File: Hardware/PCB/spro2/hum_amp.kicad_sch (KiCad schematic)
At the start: 5 parts, among them U4 ${SIM.PARAMS}

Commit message: Updated schematic and 1st version of the PCB
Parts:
- removed U4: ${SIM.PARAMS}, symbol Simulation_SPICE:OPAMP
- added C3: 4.7u, Capacitor_THT:CP_Radial_D5.0mm_P2.00mm, symbol Device:C
- added R4: 3.3, Resistor_THT:R_Axial_DIN0207_L6.3mm_D2.5mm_P10.16mm_Horizontal, symbol Device:R
- added U3: TL074, SPRO_lib:DIP794W53P254L1930H508Q14N, symbol Amplifier_Operational:TL074
- R5: renamed from R4; footprint (none) -> Resistor_THT:R_Axial_DIN0207_L6.3mm_D2.5mm_P10.16mm_Horizontal
- R6: renamed from R5; footprint (none) -> Resistor_THT:R_Axial_DIN0207_L6.3mm_D2.5mm_P10.16mm_Horizontal
- R7: renamed from R6; footprint (none) -> Resistor_THT:R_Axial_DIN0207_L6.3mm_D2.5mm_P10.16mm_Horizontal
- R8: renamed from R7; footprint (none) -> Resistor_THT:R_Axial_DIN0207_L6.3mm_D2.5mm_P10.16mm_Horizontal
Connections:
- net GND: now also C3.2
- net Hum_Amp__Out: now also U3.14
- net Humidity_In: now also R4.1; no longer R6.1
- net at R7.2, R8.1: now also U3.12 (+)
- net at R5.2, R6.2: now also U3.13 (-)
- new net: C3.1, R4.2, R6.1

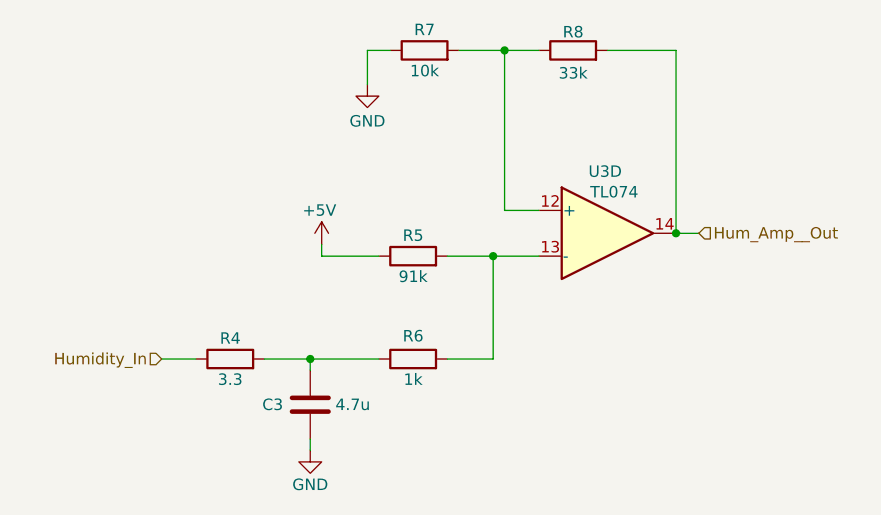
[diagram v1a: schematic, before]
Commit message: Changes to humidity circuit. Add MAX660 circuit
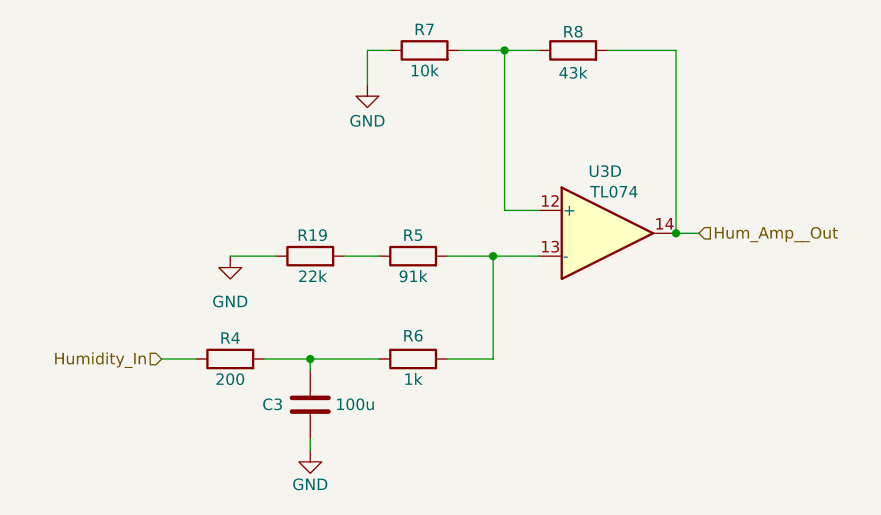
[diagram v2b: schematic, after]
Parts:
- added R19: 22k, symbol Device:R
- C3: value 4.7u -> 100u
- R4: value 3.3 -> 200
- R8: value 33k -> 43k
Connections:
- net GND: now also R19.1
- net +5V: no longer names the net of R5.1
- net +5V: now also R19.2
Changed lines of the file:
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@@
-	(wire
-		(pts
-			(xy 130.81 91.44) (xy 137.16 91.44)
-		)
-		(stroke
-			(width 0)
-			(type default)
-		)
-	)
 	(wire
 		(pts
@@
 	(wire
 		(pts
+			(xy 133.35 91.44) (xy 137.16 91.44)
+		)
+		(stroke
+			(width 0)
+			(type default)
+		)
+	)
+	(wire
+		(pts
 			(xy 124.46 102.87) (xy 129.54 102.87)
 		)
@@
 	(wire
 		(pts
-			(xy 130.81 90.17) (xy 130.81 91.44)
-		)
-		(stroke
-			(width 0)
-			(type default)
-		)
-	)
-	(wire
-		(pts
 			(xy 135.89 68.58) (xy 138.43 68.58)
 		)
@@
 		(pts
 			(xy 113.03 102.87) (xy 116.84 102.87)
+		)
+		(stroke
+			(width 0)
+			(type default)
+		)
+	)
+	(wire
+		(pts
+			(xy 120.65 91.44) (xy 125.73 91.44)
 		)
 		(stroke
@@
 	)
 	(symbol
+		(lib_id "power:GND")
+		(at 120.65 91.44 0)
+		(unit 1)
+		(exclude_from_sim no)
+		(in_bom yes)
+		(on_board yes)
+		(dnp no)
+		(fields_autoplaced yes)
+		(property "Reference" "#PWR017"
+			(at 120.65 97.79 0)
+			(effects
+				(font
+					(size 1.27 1.27)
+				)
+				(hide yes)
+			)
+		)
+		(property "Value" "GND"
+			(at 120.65 96.52 0)
+			(effects
+				(font
+					(size 1.27 1.27)
+				)
+			)
+		)
+		(property "Footprint" ""
+			(at 120.65 91.44 0)
+			(effects
+				(font
+					(size 1.27 1.27)
+				)
+				(hide yes)
+			)
+		)
+		(property "Datasheet" ""
+			(at 120.65 91.44 0)
+			(effects
+				(font
+					(size 1.27 1.27)
+				)
+				(hide yes)
+			)
+		)
+		(property "Description" "Power symbol creates a global label with name \"GND\" , ground"
+			(at 120.65 91.44 0)
+			(effects
+				(font
+					(size 1.27 1.27)
+				)
+				(hide yes)
+			)
+		)
+		(pin "1"
+		)
+		(instances
+			(project ""
+				(path "/edfea366-2226-45cc-893f-1155e0ffe333/714514db-32eb-40cc-b906-bb659214b924"
+					(reference "#PWR017")
+					(unit 1)
+				)
+			)
+		)
+	)
+	(symbol
 		(lib_id "Amplifier_Operational:TL074")
 		(at 162.56 88.9 0)
@@
 	)
 	(symbol
-		(lib_id "power:+5V")
-		(at 130.81 90.17 0)
-		(unit 1)
-		(exclude_from_sim no)
-		(in_bom yes)
-		(on_board yes)
-		(dnp no)
-		(property "Reference" "#PWR017"
-			(at 130.81 93.98 0)
-			(effects
-				(font
-					(size 1.27 1.27)
-				)
-				(hide yes)
-			)
-		)
-		(property "Value" "+5V"
-			(at 130.556 86.36 0)
-			(effects
-				(font
-					(size 1.27 1.27)
-				)
-			)
-		)
-		(property "Footprint" ""
-			(at 130.81 90.17 0)
-			(effects
-				(font
-					(size 1.27 1.27)
-				)
-				(hide yes)
-			)
-		)
-		(property "Datasheet" ""
-			(at 130.81 90.17 0)
-			(effects
-				(font
-					(size 1.27 1.27)
-				)
-				(hide yes)
-			)
-		)
-		(property "Description" "Power symbol creates a global label with name \"+5V\""
-			(at 130.81 90.17 0)
-			(effects
-				(font
-					(size 1.27 1.27)
-				)
-				(hide yes)
-			)
-		)
-		(pin "1"
-		)
-		(instances
-			(project "spro2"
-				(path "/edfea366-2226-45cc-893f-1155e0ffe333/714514db-32eb-40cc-b906-bb659214b924"
-					(reference "#PWR017")
-					(unit 1)
-				)
-			)
-		)
-	)
-	(symbol
 		(lib_id "power:GND")
 		(at 135.89 72.39 0)
@@
 	)
 	(symbol
+		(lib_id "Device:R")
+		(at 129.54 91.44 90)
+		(unit 1)
+		(exclude_from_sim no)
+		(in_bom yes)
+		(on_board yes)
+		(dnp no)
+		(property "Reference" "R19"
+			(at 129.794 89.154 90)
+			(effects
+				(font
+					(size 1.27 1.27)
+				)
+			)
+		)
+		(property "Value" "22k"
+			(at 129.794 93.726 90)
+			(effects
+				(font
+					(size 1.27 1.27)
+				)
+			)
+		)
+		(property "Footprint" ""
+			(at 129.54 93.218 90)
+			(effects
+				(font
+					(size 1.27 1.27)
+				)
+				(hide yes)
+			)
+		)
+		(property "Datasheet" "~"
+			(at 129.54 91.44 0)
+			(effects
+				(font
+					(size 1.27 1.27)
+				)
+				(hide yes)
+			)
+		)
+		(property "Description" "Resistor"
+			(at 129.54 91.44 0)
+			(effects
+				(font
+					(size 1.27 1.27)
+				)
+				(hide yes)
+			)
+		)
+		(pin "1"
+		)
+		(pin "2"
+		)
+		(instances
+			(project ""
+				(path "/edfea366-2226-45cc-893f-1155e0ffe333/714514db-32eb-40cc-b906-bb659214b924"
+					(reference "R19")
+					(unit 1)
+				)
+			)
+		)
+	)
+	(symbol
 		(lib_id "Device:C")
 		(at 129.54 107.95 0)
@@
 			)
 		)
-		(property "Value" "4.7u"
+		(property "Value" "100u"
 			(at 132.334 107.95 0)
 			(effects
@@
 			)
 		)
-		(property "Value" "33k"
+		(property "Value" "43k"
 			(at 158.75 71.12 90)
 			(effects
@@
 			)
 		)
-		(property "Value" "3.3"
+		(property "Value" "200"
 			(at 120.65 105.156 90)
 			(effects

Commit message: Hopefully last version of PCB
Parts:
- removed C3: 100u, Capacitor_THT:CP_Radial_D5.0mm_P2.00mm, symbol Device:C
- added C7: 100u, Capacitor_THT:CP_Radial_D10.0mm_P5.00mm, symbol Device:C_Polarized
- R6: renamed from R19; footprint (none) -> Resistor_THT:R_Axial_DIN0207_L6.3mm_D2.5mm_P10.16mm_Horizontal
- renumbered R8 to R10, R4 to R5, R5 to R7, R6 to R8, R7 to R9
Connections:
- net GND: now also C7.2
- net at R5.2, R8.1: now also C7.1
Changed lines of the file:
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@@
+	)
+	(symbol
+		(lib_id "Device:C_Polarized")
+		(at 129.54 107.95 0)
+		(unit 1)
+		(exclude_from_sim no)
+		(in_bom yes)
+		(on_board yes)
+		(dnp no)
+		(fields_autoplaced yes)
+		(property "Reference" "C7"
+			(at 133.35 105.7909 0)
+			(effects
+				(font
+					(size 1.27 1.27)
+				)
+				(justify left)
+			)
+		)
+		(property "Value" "100u"
+			(at 133.35 108.3309 0)
+			(effects
+				(font
+					(size 1.27 1.27)
+				)
+				(justify left)
+			)
+		)
+		(property "Footprint" "Capacitor_THT:CP_Radial_D10.0mm_P5.00mm"
+			(at 130.5052 111.76 0)
+			(effects
+				(font
+					(size 1.27 1.27)
+				)
+				(hide yes)
+			)
+		)
+		(property "Datasheet" "~"
+			(at 129.54 107.95 0)
+			(effects
+				(font
+					(size 1.27 1.27)
+				)
+				(hide yes)
+			)
+		)
+		(property "Description" "Polarized capacitor"
+			(at 129.54 107.95 0)
+			(effects
+				(font
+					(size 1.27 1.27)
+				)
+				(hide yes)
+			)
+		)
+		(pin "1"
+		)
+		(pin "2"
+		)
+		(instances
+			(project "spro2"
+				(path "/edfea366-2226-45cc-893f-1155e0ffe333/714514db-32eb-40cc-b906-bb659214b924"
+					(reference "C7")
+					(unit 1)
+				)
+			)
+		)
 	)
 	(symbol
@@
 		(on_board yes)
 		(dnp no)
-		(property "Reference" "#PWR016"
+		(property "Reference" "#PWR018"
 			(at 129.54 119.38 0)
 			(effects
@@
 			(project "spro2"
 				(path "/edfea366-2226-45cc-893f-1155e0ffe333/714514db-32eb-40cc-b906-bb659214b924"
-					(reference "#PWR016")
+					(reference "#PWR018")
 					(unit 1)
 				)
@@
 		(on_board yes)
 		(dnp no)
-		(property "Reference" "#PWR018"
+		(property "Reference" "#PWR019"
 			(at 135.89 78.74 0)
 			(effects
@@
 			(project "spro2"
 				(path "/edfea366-2226-45cc-893f-1155e0ffe333/714514db-32eb-40cc-b906-bb659214b924"
-					(reference "#PWR018")
+					(reference "#PWR019")
 					(unit 1)
 				)
@@
 		(on_board yes)
 		(dnp no)
-		(property "Reference" "R19"
+		(property "Reference" "R6"
 			(at 129.794 89.154 90)
 			(effects
@@
 			)
 		)
-		(property "Footprint" ""
+		(property "Footprint" "Resistor_THT:R_Axial_DIN0207_L6.3mm_D2.5mm_P10.16mm_Horizontal"
 			(at 129.54 93.218 90)
 			(effects
@@
 			(project ""
 				(path "/edfea366-2226-45cc-893f-1155e0ffe333/714514db-32eb-40cc-b906-bb659214b924"
-					(reference "R19")
-					(unit 1)
-				)
-			)
-		)
-	)
-	(symbol
-		(lib_id "Device:C")
-		(at 129.54 107.95 0)
-		(unit 1)
-		(exclude_from_sim no)
-		(in_bom yes)
-		(on_board yes)
-		(dnp no)
-		(property "Reference" "C3"
-			(at 124.206 107.95 0)
-			(effects
-				(font
-					(size 1.27 1.27)
-				)
-				(justify left)
-			)
-		)
-		(property "Value" "100u"
-			(at 132.334 107.95 0)
-			(effects
-				(font
-					(size 1.27 1.27)
-				)
-				(justify left)
-			)
-		)
-		(property "Footprint" "Capacitor_THT:CP_Radial_D5.0mm_P2.00mm"
-			(at 130.5052 111.76 0)
-			(effects
-				(font
-					(size 1.27 1.27)
-				)
-				(hide yes)
-			)
-		)
-		(property "Datasheet" "~"
-			(at 129.54 107.95 0)
-			(effects
-				(font
-					(size 1.27 1.27)
-				)
-				(hide yes)
-			)
-		)
-		(property "Description" "Unpolarized capacitor"
-			(at 129.54 107.95 0)
-			(effects
-				(font
-					(size 1.27 1.27)
-				)
-				(hide yes)
-			)
-		)
-		(pin "2"
-		)
-		(pin "1"
-		)
-		(instances
-			(project "spro2"
-				(path "/edfea366-2226-45cc-893f-1155e0ffe333/714514db-32eb-40cc-b906-bb659214b924"
-					(reference "C3")
+					(reference "R6")
 					(unit 1)
 				)
@@
 		(on_board yes)
 		(dnp no)
-		(property "Reference" "R7"
+		(property "Reference" "R9"
 			(at 142.24 66.294 90)
 			(effects
@@
 			(project "spro2"
 				(path "/edfea366-2226-45cc-893f-1155e0ffe333/714514db-32eb-40cc-b906-bb659214b924"
-					(reference "R7")
+					(reference "R9")
 					(unit 1)
 				)
@@
 		(on_board yes)
 		(dnp no)
-		(property "Reference" "R5"
+		(property "Reference" "R7"
 			(at 140.97 89.154 90)
 			(effects
@@
 			(project "spro2"
 				(path "/edfea366-2226-45cc-893f-1155e0ffe333/714514db-32eb-40cc-b906-bb659214b924"
-					(reference "R5")
+					(reference "R7")
 					(unit 1)
 				)
@@
 		(on_board yes)
 		(dnp no)
-		(property "Reference" "R6"
+		(property "Reference" "R8"
 			(at 140.97 100.33 90)
 			(effects
@@
 			(project "spro2"
 				(path "/edfea366-2226-45cc-893f-1155e0ffe333/714514db-32eb-40cc-b906-bb659214b924"
-					(reference "R6")
+					(reference "R8")
 					(unit 1)
 				)
@@
 		(on_board yes)
 		(dnp no)
-		(property "Reference" "R8"
+		(property "Reference" "R10"
 			(at 158.75 66.548 90)
 			(effects
@@
 			(project "spro2"
 				(path "/edfea366-2226-45cc-893f-1155e0ffe333/714514db-32eb-40cc-b906-bb659214b924"
-					(reference "R8")
+					(reference "R10")
 					(unit 1)
 				)
@@
 		(on_board yes)
 		(dnp no)
-		(property "Reference" "R4"
+		(property "Reference" "R5"
 			(at 120.65 100.584 90)
 			(effects
@@
 			(project "spro2"
 				(path "/edfea366-2226-45cc-893f-1155e0ffe333/714514db-32eb-40cc-b906-bb659214b924"
-					(reference "R4")
-					(unit 1)
-				)
+					(reference "R5")
+					(unit 1)
+				)

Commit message: Final scheamtic mega trust
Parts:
- R10: value 43k -> 33k
- R5: value 200 -> 2k
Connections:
- net GND: no longer R6.1
- net at R10.1, R9.2: now also U3.13 (-); no longer U3.12 (+)
- net at R7.2, R8.2: now also U3.12 (+); no longer U3.13 (-)
- new net +5V: R6.1
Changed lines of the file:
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@@
+	(wire
+		(pts
+			(xy 120.65 88.9) (xy 120.65 91.44)
+		)
+		(stroke
+			(width 0)
+			(type default)
+		)
+	)
 	(wire
 		(pts
@@
 		(on_board yes)
 		(dnp no)
-		(fields_autoplaced yes)
 		(property "Reference" "C7"
 			(at 133.35 105.7909 0)
@@
 	)
 	(symbol
-		(lib_id "power:GND")
-		(at 120.65 91.44 0)
-		(unit 1)
-		(exclude_from_sim no)
-		(in_bom yes)
-		(on_board yes)
-		(dnp no)
-		(fields_autoplaced yes)
+		(lib_id "Amplifier_Operational:TL074")
+		(at 162.56 88.9 0)
+		(mirror x)
+		(unit 4)
+		(exclude_from_sim no)
+		(in_bom yes)
+		(on_board yes)
+		(dnp no)
+		(property "Reference" "U3"
+			(at 162.306 95.758 0)
+			(effects
+				(font
+					(size 1.27 1.27)
+				)
+			)
+		)
+		(property "Value" "TL074"
+			(at 163.322 93.472 0)
+			(effects
+				(font
+					(size 1.27 1.27)
+				)
+			)
+		)
+		(property "Footprint" "SPRO_lib:DIP794W53P254L1930H508Q14N"
+			(at 161.29 91.44 0)
+			(effects
+				(font
+					(size 1.27 1.27)
+				)
+				(hide yes)
+			)
+		)
+		(property "Datasheet" "http://www.ti.com/lit/ds/symlink/tl071.pdf"
+			(at 163.83 93.98 0)
+			(effects
+				(font
+					(size 1.27 1.27)
+				)
+				(hide yes)
+			)
+		)
+		(property "Description" "Quad Low-Noise JFET-Input Operational Amplifiers, DIP-14/SOIC-14"
+			(at 162.56 88.9 0)
+			(effects
+				(font
+					(size 1.27 1.27)
+				)
+				(hide yes)
+			)
+		)
+		(pin "3"
+		)
+		(pin "11"
+		)
+		(pin "6"
+		)
+		(pin "12"
+		)
+		(pin "14"
+		)
+		(pin "4"
+		)
+		(pin "7"
+		)
+		(pin "10"
+		)
+		(pin "9"
+		)
+		(pin "5"
+		)
+		(pin "1"
+		)
+		(pin "2"
+		)
+		(pin "8"
+		)
+		(pin "13"
+		)
+		(instances
+			(project "spro2"
+				(path "/edfea366-2226-45cc-893f-1155e0ffe333/714514db-32eb-40cc-b906-bb659214b924"
+					(reference "U3")
+					(unit 4)
+				)
+			)
+		)
+	)
+	(symbol
+		(lib_id "power:+5V")
+		(at 120.65 88.9 0)
+		(unit 1)
+		(exclude_from_sim no)
+		(in_bom yes)
+		(on_board yes)
+		(dnp no)
 		(property "Reference" "#PWR017"
-			(at 120.65 97.79 0)
-			(effects
-				(font
-					(size 1.27 1.27)
-				)
-				(hide yes)
-			)
-		)
-		(property "Value" "GND"
-			(at 120.65 96.52 0)
+			(at 120.65 92.71 0)
+			(effects
+				(font
+					(size 1.27 1.27)
+				)
+				(hide yes)
+			)
+		)
+		(property "Value" "+5V"
+			(at 120.65 85.09 0)
 			(effects
 				(font
@@
 		)
 		(property "Footprint" ""
-			(at 120.65 91.44 0)
+			(at 120.65 88.9 0)
 			(effects
 				(font
@@
 		)
 		(property "Datasheet" ""
-			(at 120.65 91.44 0)
-			(effects
-				(font
-					(size 1.27 1.27)
-				)
-				(hide yes)
-			)
-		)
-		(property "Description" "Power symbol creates a global label with name \"GND\" , ground"
-			(at 120.65 91.44 0)
-			(effects
-				(font
-					(size 1.27 1.27)
-				)
-				(hide yes)
-			)
-		)
-		(pin "1"
-		)
-		(instances
-			(project ""
+			(at 120.65 88.9 0)
+			(effects
+				(font
+					(size 1.27 1.27)
+				)
+				(hide yes)
+			)
+		)
+		(property "Description" "Power symbol creates a global label with name \"+5V\""
+			(at 120.65 88.9 0)
+			(effects
+				(font
+					(size 1.27 1.27)
+				)
+				(hide yes)
+			)
+		)
+		(pin "1"
+		)
+		(instances
+			(project "spro2"
 				(path "/edfea366-2226-45cc-893f-1155e0ffe333/714514db-32eb-40cc-b906-bb659214b924"
 					(reference "#PWR017")
@@
 	)
 	(symbol
-		(lib_id "Amplifier_Operational:TL074")
-		(at 162.56 88.9 0)
-		(unit 4)
-		(exclude_from_sim no)
-		(in_bom yes)
-		(on_board yes)
-		(dnp no)
-		(property "Reference" "U3"
-			(at 162.306 82.042 0)
-			(effects
-				(font
-					(size 1.27 1.27)
-				)
-			)
-		)
-		(property "Value" "TL074"
-			(at 163.322 84.328 0)
-			(effects
-				(font
-					(size 1.27 1.27)
-				)
-			)
-		)
-		(property "Footprint" "SPRO_lib:DIP794W53P254L1930H508Q14N"
-			(at 161.29 86.36 0)
-			(effects
-				(font
-					(size 1.27 1.27)
-				)
-				(hide yes)
-			)
-		)
-		(property "Datasheet" "http://www.ti.com/lit/ds/symlink/tl071.pdf"
-			(at 163.83 83.82 0)
-			(effects
-				(font
-					(size 1.27 1.27)
-				)
-				(hide yes)
-			)
-		)
-		(property "Description" "Quad Low-Noise JFET-Input Operational Amplifiers, DIP-14/SOIC-14"
-			(at 162.56 88.9 0)
-			(effects
-				(font
-					(size 1.27 1.27)
-				)
-				(hide yes)
-			)
-		)
-		(pin "3"
-		)
-		(pin "11"
-		)
-		(pin "6"
-		)
-		(pin "12"
-		)
-		(pin "14"
-		)
-		(pin "4"
-		)
-		(pin "7"
-		)
-		(pin "10"
-		)
-		(pin "9"
-		)
-		(pin "5"
-		)
-		(pin "1"
-		)
-		(pin "2"
-		)
-		(pin "8"
-		)
-		(pin "13"
-		)
-		(instances
-			(project "spro2"
-				(path "/edfea366-2226-45cc-893f-1155e0ffe333/714514db-32eb-40cc-b906-bb659214b924"
-					(reference "U3")
-					(unit 4)
-				)
-			)
-		)
-	)
-	(symbol
 		(lib_id "power:GND")
 		(at 135.89 72.39 0)
@@
 		)
 		(property "Value" "91k"
-			(at 140.97 93.726 90)
+			(at 140.97 93.98 90)
 			(effects
 				(font
@@
 			)
 		)
-		(property "Value" "43k"
+		(property "Value" "33k"
 			(at 158.75 71.12 90)
 			(effects
@@
 			)
 		)
-		(property "Value" "200"
+		(property "Value" "2k"
 			(at 120.65 105.156 90)
 			(effects

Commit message: skibiduicide
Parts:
- R10: value 33k -> 39k
- R6: value 22k -> 9.1k
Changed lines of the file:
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@@
 			)
 		)
-		(property "Value" "22k"
+		(property "Value" "9.1k"
 			(at 129.794 93.726 90)
 			(effects
@@
 			)
 		)
-		(property "Value" "33k"
+		(property "Value" "39k"
 			(at 158.75 71.12 90)
 			(effects
